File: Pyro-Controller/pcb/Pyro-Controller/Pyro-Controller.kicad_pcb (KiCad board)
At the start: 2 copper layers, 26.9 x 26.9 mm, 11 parts, among them J1 Screw_Terminal_01x02, J2 Conn_01x03_Socket, Q1 SiS454DN

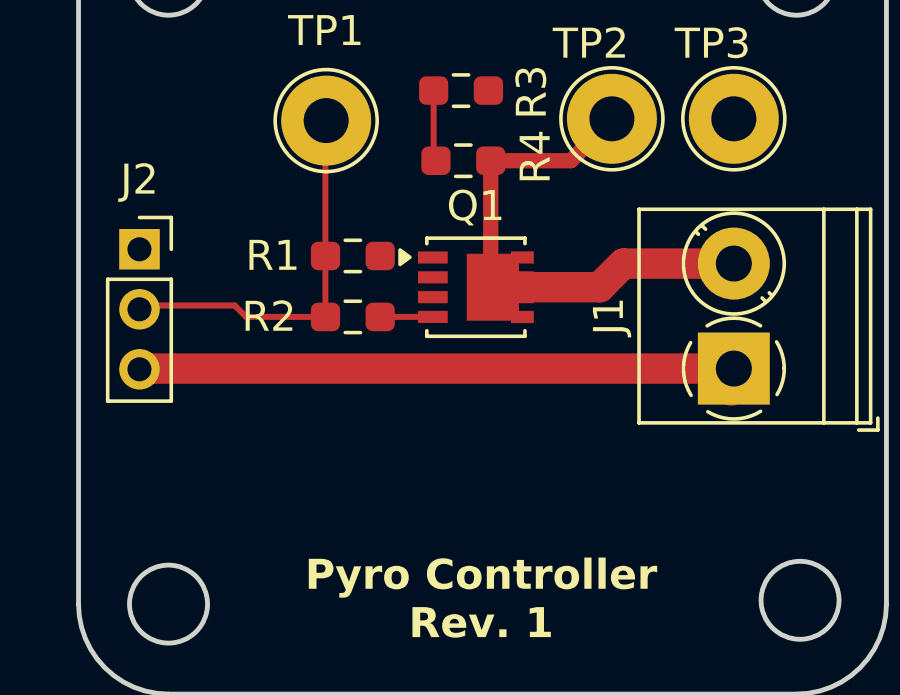
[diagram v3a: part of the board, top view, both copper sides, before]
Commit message: Fiducial schematic symbols. Position, gerber, and drill files generation
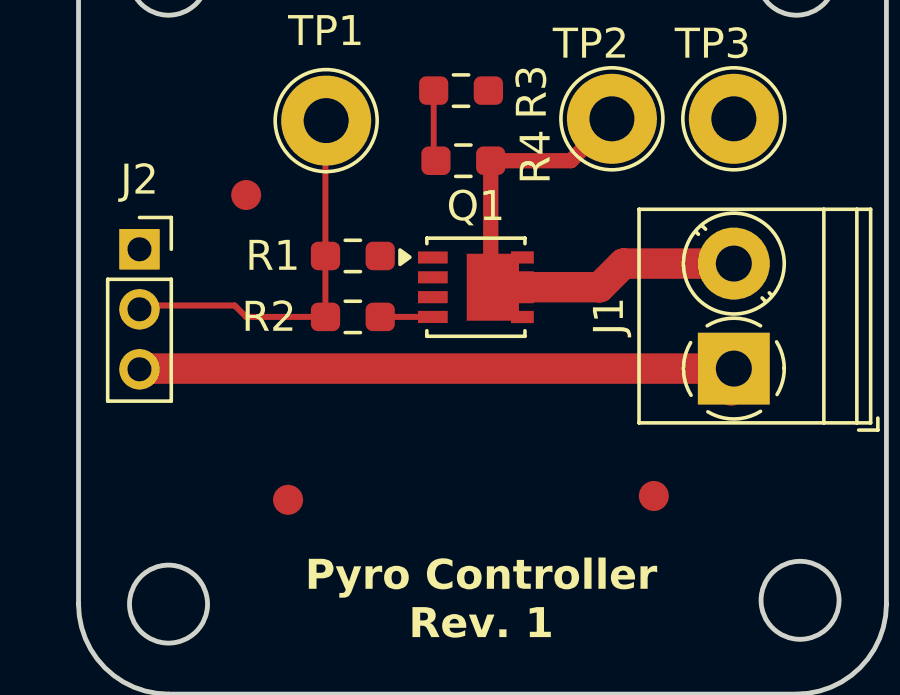
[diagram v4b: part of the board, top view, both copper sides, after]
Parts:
- added FID1: Fiducial, Fiducial:Fiducial_1mm_Mask2mm, F.Cu at (30.6, 38.0)
- added FID2: Fiducial, Fiducial:Fiducial_1mm_Mask2mm, F.Cu at (29.2, 27.8)
- added FID3: Fiducial, Fiducial:Fiducial_1mm_Mask2mm, F.Cu at (42.8, 37.8)

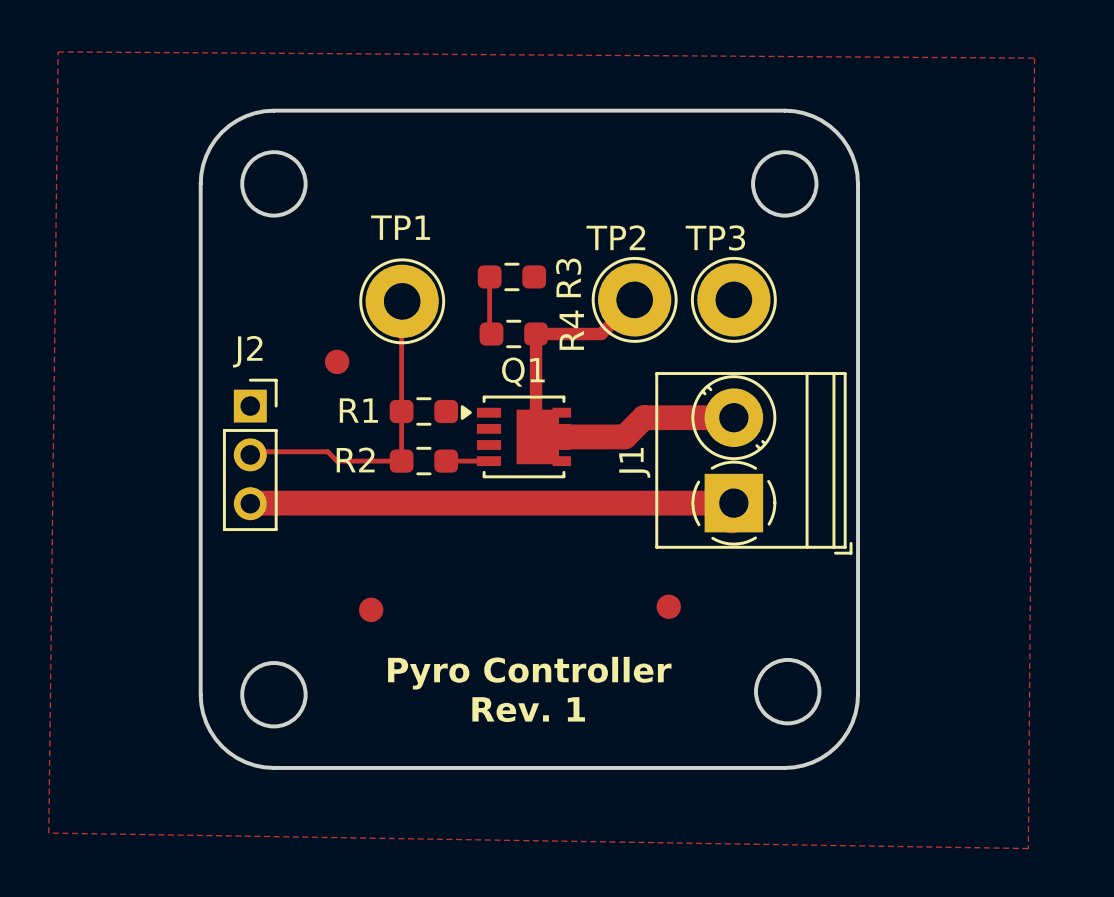
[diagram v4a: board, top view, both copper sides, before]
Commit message: Fixed connector pitch (now 2.54mm) on pyro and valve controllers
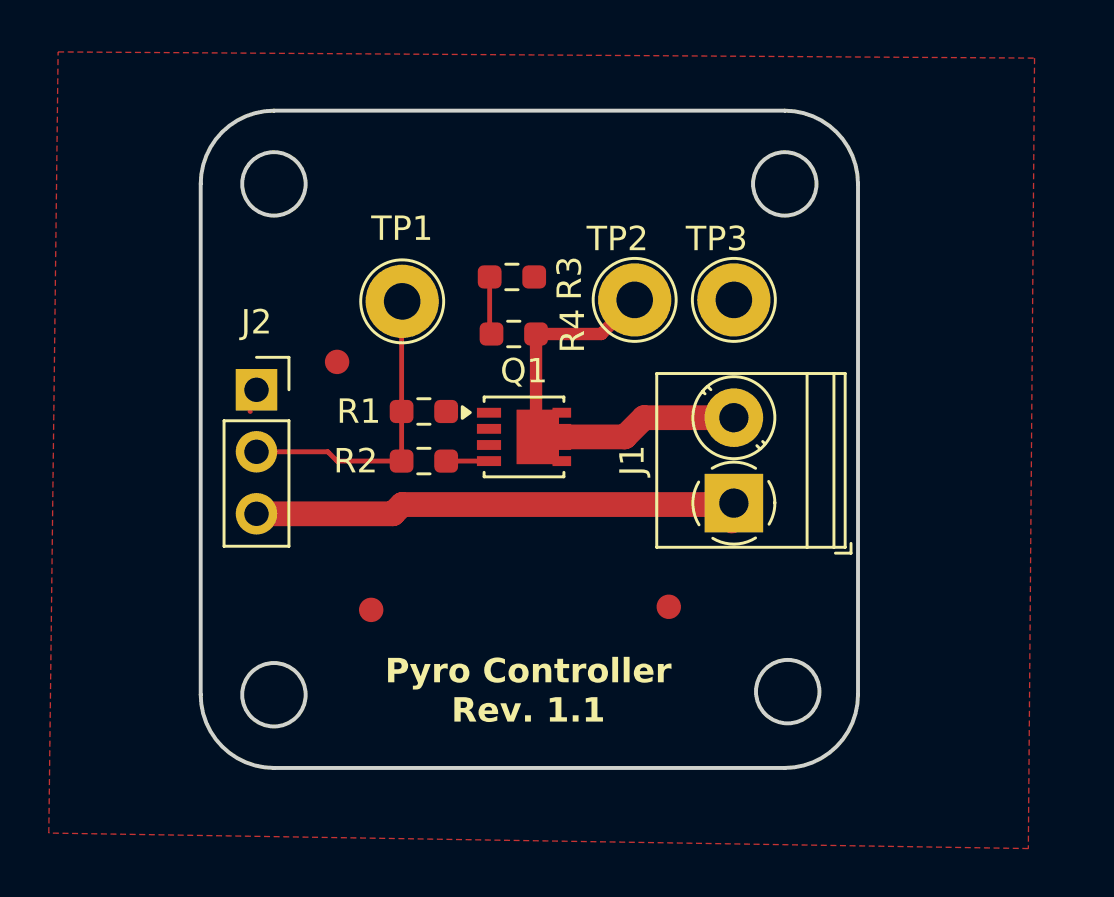
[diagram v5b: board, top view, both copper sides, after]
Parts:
- J2: footprint Connector_PinSocket_2.00mm:PinSocket_1x03_P2.00mm_Vertical -> Connector_PinSocket_2.54mm:PinSocket_1x03_P2.54mm_Vertical
- moved J2 0.71 mm to (25.9, 29.0)
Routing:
- net +3.3V: track 20.4 -> 20.9 mm
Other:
- board text added: "Pyro Controller Rev. 1.1"
- board text removed: "Pyro Controller Rev. 1"
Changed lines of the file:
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@@
 		)
 	)
-	(footprint "Connector_PinSocket_2.00mm:PinSocket_1x03_P2.00mm_Vertical"
+	(footprint "Connector_PinSocket_2.54mm:PinSocket_1x03_P2.54mm_Vertical"
 		(layer "F.Cu")
-		(at 25.654 29.623)
-		(descr "Through hole straight socket strip, 1x03, 2.00mm pitch, single row (from Kicad 4.0.7), script generated")
-		(tags "Through hole socket strip THT 1x03 2.00mm single row")
+		(at 25.908 28.956)
+		(descr "Through hole straight socket strip, 1x03, 2.54mm pitch, single row (from Kicad 4.0.7), script generated")
+		(tags "Through hole socket strip THT 1x03 2.54mm single row")
 		(property "Reference" "J2"
-			(at 0 -2.318 0)
+			(at 0 -2.77 0)
 			(layer "F.SilkS")
 			(effects
@@
 		)
 		(property "Value" "Conn_01x03_Socket"
-			(at 0 6.5 0)
+			(at 0 7.85 0)
 			(layer "F.Fab")
 			(effects
@@
 			)
 		)
-		(property "Footprint" "Connector_PinSocket_2.00mm:PinSocket_1x03_P2.00mm_Vertical"
+		(property "Footprint" "Connector_PinSocket_2.54mm:PinSocket_1x03_P2.54mm_Vertical"
 			(at 0 0 0)
 			(unlocked yes)
@@
 		(attr through_hole)
 		(fp_line
-			(start -1.06 1)
-			(end -1.06 5.06)
+			(start -1.33 1.27)
+			(end -1.33 6.41)
 			(stroke
 				(width 0.12)
@@
 		)
 		(fp_line
-			(start -1.06 1)
-			(end 1.06 1)
+			(start -1.33 1.27)
+			(end 1.33 1.27)
 			(stroke
 				(width 0.12)
@@
 		)
 		(fp_line
-			(start -1.06 5.06)
-			(end 1.06 5.06)
+			(start -1.33 6.41)
+			(end 1.33 6.41)
 			(stroke
 				(width 0.12)
@@
 		)
 		(fp_line
-			(start 0 -1.06)
-			(end 1.06 -1.06)
+			(start 0 -1.33)
+			(end 1.33 -1.33)
 			(stroke
 				(width 0.12)
@@
 		)
 		(fp_line
-			(start 1.06 -1.06)
-			(end 1.06 0)
+			(start 1.33 -1.33)
+			(end 1.33 0)
 			(stroke
 				(width 0.12)
@@
 		)
 		(fp_line
-			(start 1.06 1)
-			(end 1.06 5.06)
+			(start 1.33 1.27)
+			(end 1.33 6.41)
 			(stroke
 				(width 0.12)
@@
 		)
 		(fp_line
-			(start -1.5 -1.5)
-			(end 1.5 -1.5)
+			(start -1.8 -1.8)
+			(end 1.75 -1.8)
 			(stroke
 				(width 0.05)
@@
 		)
 		(fp_line
-			(start -1.5 5.5)
-			(end -1.5 -1.5)
+			(start -1.8 6.85)
+			(end -1.8 -1.8)
 			(stroke
 				(width 0.05)
@@
 		)
 		(fp_line
-			(start 1.5 -1.5)
-			(end 1.5 5.5)
+			(start 1.75 -1.8)
+			(end 1.75 6.85)
 			(stroke
 				(width 0.05)
@@
 		)
 		(fp_line
-			(start 1.5 5.5)
-			(end -1.5 5.5)
+			(start 1.75 6.85)
+			(end -1.8 6.85)
 			(stroke
 				(width 0.05)
@@
 		)
 		(fp_line
-			(start -1 -1)
-			(end 0.5 -1)
+			(start -1.27 -1.27)
+			(end 0.635 -1.27)
 			(stroke
 				(width 0.1)
@@
 		)
 		(fp_line
-			(start -1 5)
-			(end -1 -1)
+			(start -1.27 6.35)
+			(end -1.27 -1.27)
 			(stroke
 				(width 0.1)
@@
 		)
 		(fp_line
-			(start 0.5 -1)
-			(end 1 -0.5)
+			(start 0.635 -1.27)
+			(end 1.27 -0.635)
 			(stroke
 				(width 0.1)
@@
 		)
 		(fp_line
-			(start 1 -0.5)
-			(end 1 5)
+			(start 1.27 -0.635)
+			(end 1.27 6.35)
 			(stroke
 				(width 0.1)
@@
 		)
 		(fp_line
-			(start 1 5)
-			(end -1 5)
+			(start 1.27 6.35)
+			(end -1.27 6.35)
 			(stroke
 				(width 0.1)
@@
 		)
 		(fp_text user "${REFERENCE}"
-			(at 0 2 90)
+			(at 0 2.54 90)
 			(layer "F.Fab")
 			(effects
@@
 		(pad "1" thru_hole rect
 			(at 0 0)
-			(size 1.35 1.35)
-			(drill 0.8)
+			(size 1.7 1.7)
+			(drill 1)
 			(layers "*.Cu" "*.Mask")
 			(remove_unused_layers no)
@@
 		)
 		(pad "2" thru_hole oval
-			(at 0 2)
-			(size 1.35 1.35)
-			(drill 0.8)
+			(at 0 2.54)
+			(size 1.7 1.7)
+			(drill 1)
 			(layers "*.Cu" "*.Mask")
 			(remove_unused_layers no)
@@
 		)
 		(pad "3" thru_hole oval
-			(at 0 4)
-			(size 1.35 1.35)
-			(drill 0.8)
+			(at 0 5.08)
+			(size 1.7 1.7)
+			(drill 1)
 			(layers "*.Cu" "*.Mask")
 			(remove_unused_layers no)
@@
 			(pintype "passive")
 		)
-		(model "${KICAD8_3DMODEL_DIR}/Connector_PinSocket_2.00mm.3dshapes/PinSocket_1x03_P2.00mm_Vertical.wrl"
+		(model "${KICAD8_3DMODEL_DIR}/Connector_PinSocket_2.54mm.3dshapes/PinSocket_1x03_P2.54mm_Vertical.wrl"
 			(offset
 				(xyz 0 0 0)
@@
 		(layer "Edge.Cuts")
 	)
-	(gr_text "Pyro Controller\nRev. 1"
+	(gr_text "Pyro Controller\nRev. 1.1"
 		(at 37.043404 42.672 0)
 		(layer "B.SilkS")
@@
 		)
 	)
-	(gr_text "Pyro Controller\nRev. 1"
-		(at 37.043404 42.672 -0)
+	(gr_text "Pyro Controller\nRev. 1.1"
+		(at 37.043404 42.672 0)
 		(layer "F.SilkS")
 		(effects
@@
 	)
 	(segment
-		(start 45.466 33.599)
-		(end 25.964 33.599)
+		(start 31.496 34.036)
+		(end 25.679 34.036)
 		(width 1.016)
 		(layer "F.Cu")
@@
 	)
 	(segment
-		(start 25.964 33.599)
-		(end 25.908 33.655)
+		(start 31.87425 33.65775)
+		(end 31.496 34.036)
+		(width 1.016)
+		(layer "F.Cu")
+		(net 1)
+	)
+	(segment
+		(start 25.679 34.036)
+		(end 25.679 33.884)
 		(width 1.016)
 		(layer "F.Cu")
@@
 		(width 1.016)
 		(layer "F.Cu")
+		(net 1)
+	)
+	(segment
+		(start 45.40725 33.65775)
+		(end 31.87425 33.65775)
+		(width 1.016)
+		(layer "F.Cu")
+		(net 1)
+	)
+	(segment
+		(start 45.466 33.599)
+		(end 45.40725 33.65775)
+		(width 1.016)
+		(layer "F.Cu")

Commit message: Revert "Resolved recovery dev merge"
This reverts commit 81c4bbda93894cf9b120906f02d3dbab6bbd1e60, reversing
changes made to 220360569fc6c62025a0e7a68270d7f77f4a1f37.
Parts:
- J2: footprint Connector_PinSocket_2.54mm:PinSocket_1x03_P2.54mm_Vertical -> Connector_PinSocket_2.00mm:PinSocket_1x03_P2.00mm_Vertical
- moved J2 0.71 mm to (25.7, 29.6)
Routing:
- net +3.3V: track 20.9 -> 20.4 mm
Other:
- board text added: "Pyro Controller Rev. 1"
- board text removed: "Pyro Controller Rev. 1.1"
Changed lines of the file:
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@@
 		)
 	)
-	(footprint "Connector_PinSocket_2.54mm:PinSocket_1x03_P2.54mm_Vertical"
+	(footprint "Connector_PinSocket_2.00mm:PinSocket_1x03_P2.00mm_Vertical"
 		(layer "F.Cu")
-		(at 25.908 28.956)
-		(descr "Through hole straight socket strip, 1x03, 2.54mm pitch, single row (from Kicad 4.0.7), script generated")
-		(tags "Through hole socket strip THT 1x03 2.54mm single row")
+		(at 25.654 29.623)
+		(descr "Through hole straight socket strip, 1x03, 2.00mm pitch, single row (from Kicad 4.0.7), script generated")
+		(tags "Through hole socket strip THT 1x03 2.00mm single row")
 		(property "Reference" "J2"
-			(at 0 -2.77 0)
+			(at 0 -2.318 0)
 			(layer "F.SilkS")
 			(effects
@@
 		)
 		(property "Value" "Conn_01x03_Socket"
-			(at 0 7.85 0)
+			(at 0 6.5 0)
 			(layer "F.Fab")
 			(effects
@@
 			)
 		)
-		(property "Footprint" "Connector_PinSocket_2.54mm:PinSocket_1x03_P2.54mm_Vertical"
+		(property "Footprint" "Connector_PinSocket_2.00mm:PinSocket_1x03_P2.00mm_Vertical"
 			(at 0 0 0)
 			(unlocked yes)
@@
 		(attr through_hole)
 		(fp_line
-			(start -1.33 1.27)
-			(end -1.33 6.41)
+			(start -1.06 1)
+			(end -1.06 5.06)
 			(stroke
 				(width 0.12)
@@
 		)
 		(fp_line
-			(start -1.33 1.27)
-			(end 1.33 1.27)
+			(start -1.06 1)
+			(end 1.06 1)
 			(stroke
 				(width 0.12)
@@
 		)
 		(fp_line
-			(start -1.33 6.41)
-			(end 1.33 6.41)
+			(start -1.06 5.06)
+			(end 1.06 5.06)
 			(stroke
 				(width 0.12)
@@
 		)
 		(fp_line
-			(start 0 -1.33)
-			(end 1.33 -1.33)
+			(start 0 -1.06)
+			(end 1.06 -1.06)
 			(stroke
 				(width 0.12)
@@
 		)
 		(fp_line
-			(start 1.33 -1.33)
-			(end 1.33 0)
+			(start 1.06 -1.06)
+			(end 1.06 0)
 			(stroke
 				(width 0.12)
@@
 		)
 		(fp_line
-			(start 1.33 1.27)
-			(end 1.33 6.41)
+			(start 1.06 1)
+			(end 1.06 5.06)
 			(stroke
 				(width 0.12)
@@
 		)
 		(fp_line
-			(start -1.8 -1.8)
-			(end 1.75 -1.8)
+			(start -1.5 -1.5)
+			(end 1.5 -1.5)
 			(stroke
 				(width 0.05)
@@
 		)
 		(fp_line
-			(start -1.8 6.85)
-			(end -1.8 -1.8)
+			(start -1.5 5.5)
+			(end -1.5 -1.5)
 			(stroke
 				(width 0.05)
@@
 		)
 		(fp_line
-			(start 1.75 -1.8)
-			(end 1.75 6.85)
+			(start 1.5 -1.5)
+			(end 1.5 5.5)
 			(stroke
 				(width 0.05)
@@
 		)
 		(fp_line
-			(start 1.75 6.85)
-			(end -1.8 6.85)
+			(start 1.5 5.5)
+			(end -1.5 5.5)
 			(stroke
 				(width 0.05)
@@
 		)
 		(fp_line
-			(start -1.27 -1.27)
-			(end 0.635 -1.27)
+			(start -1 -1)
+			(end 0.5 -1)
 			(stroke
 				(width 0.1)
@@
 		)
 		(fp_line
-			(start -1.27 6.35)
-			(end -1.27 -1.27)
+			(start -1 5)
+			(end -1 -1)
 			(stroke
 				(width 0.1)
@@
 		)
 		(fp_line
-			(start 0.635 -1.27)
-			(end 1.27 -0.635)
+			(start 0.5 -1)
+			(end 1 -0.5)
 			(stroke
 				(width 0.1)
@@
 		)
 		(fp_line
-			(start 1.27 -0.635)
-			(end 1.27 6.35)
+			(start 1 -0.5)
+			(end 1 5)
 			(stroke
 				(width 0.1)
@@
 		)
 		(fp_line
-			(start 1.27 6.35)
-			(end -1.27 6.35)
+			(start 1 5)
+			(end -1 5)
 			(stroke
 				(width 0.1)
@@
 		)
 		(fp_text user "${REFERENCE}"
-			(at 0 2.54 90)
+			(at 0 2 90)
 			(layer "F.Fab")
 			(effects
@@
 		(pad "1" thru_hole rect
 			(at 0 0)
-			(size 1.7 1.7)
-			(drill 1)
+			(size 1.35 1.35)
+			(drill 0.8)
 			(layers "*.Cu" "*.Mask")
 			(remove_unused_layers no)
@@
 		)
 		(pad "2" thru_hole oval
-			(at 0 2.54)
-			(size 1.7 1.7)
-			(drill 1)
+			(at 0 2)
+			(size 1.35 1.35)
+			(drill 0.8)
 			(layers "*.Cu" "*.Mask")
 			(remove_unused_layers no)
@@
 		)
 		(pad "3" thru_hole oval
-			(at 0 5.08)
-			(size 1.7 1.7)
-			(drill 1)
+			(at 0 4)
+			(size 1.35 1.35)
+			(drill 0.8)
 			(layers "*.Cu" "*.Mask")
 			(remove_unused_layers no)
@@
 			(pintype "passive")
 		)
-		(model "${KICAD8_3DMODEL_DIR}/Connector_PinSocket_2.54mm.3dshapes/PinSocket_1x03_P2.54mm_Vertical.wrl"
+		(model "${KICAD8_3DMODEL_DIR}/Connector_PinSocket_2.00mm.3dshapes/PinSocket_1x03_P2.00mm_Vertical.wrl"
 			(offset
 				(xyz 0 0 0)
@@
 		(layer "Edge.Cuts")
 	)
-	(gr_text "Pyro Controller\nRev. 1.1"
+	(gr_text "Pyro Controller\nRev. 1"
 		(at 37.043404 42.672 0)
 		(layer "B.SilkS")
@@
 		)
 	)
-	(gr_text "Pyro Controller\nRev. 1.1"
-		(at 37.043404 42.672 0)
+	(gr_text "Pyro Controller\nRev. 1"
+		(at 37.043404 42.672 -0)
 		(layer "F.SilkS")
 		(effects
@@
 	)
 	(segment
-		(start 31.496 34.036)
-		(end 25.679 34.036)
+		(start 45.466 33.599)
+		(end 25.964 33.599)
 		(width 1.016)
 		(layer "F.Cu")
@@
 	)
 	(segment
-		(start 31.87425 33.65775)
-		(end 31.496 34.036)
-		(width 1.016)
-		(layer "F.Cu")
-		(net 1)
-	)
-	(segment
-		(start 25.679 34.036)
-		(end 25.679 33.884)
+		(start 25.964 33.599)
+		(end 25.908 33.655)
 		(width 1.016)
 		(layer "F.Cu")
@@
 		(width 1.016)
 		(layer "F.Cu")
-		(net 1)
-	)
-	(segment
-		(start 45.40725 33.65775)
-		(end 31.87425 33.65775)
-		(width 1.016)
-		(layer "F.Cu")
-		(net 1)
-	)
-	(segment
-		(start 45.466 33.599)
-		(end 45.40725 33.65775)
-		(width 1.016)
-		(layer "F.Cu")
